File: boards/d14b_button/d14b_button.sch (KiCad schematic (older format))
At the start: 65 parts, among them CON1 USB-MICRO-B, P1 CONN_02X05, P2 CONN_01X03, P3 PIEZO_BUZZ, P4 EEPROM_SPI, Q1 MOSFET_N, Q2 IRLM6402, Q3 BSS138, SW1 SW_PUSH, SW2 SW_PUSH, SW3 SW_PUSH, SW4 SW_PUSH, U1 nRF24L01+-Module, U2 STM32F030C8T6, U3 TPS61221, X1 8M, X2 32.768k

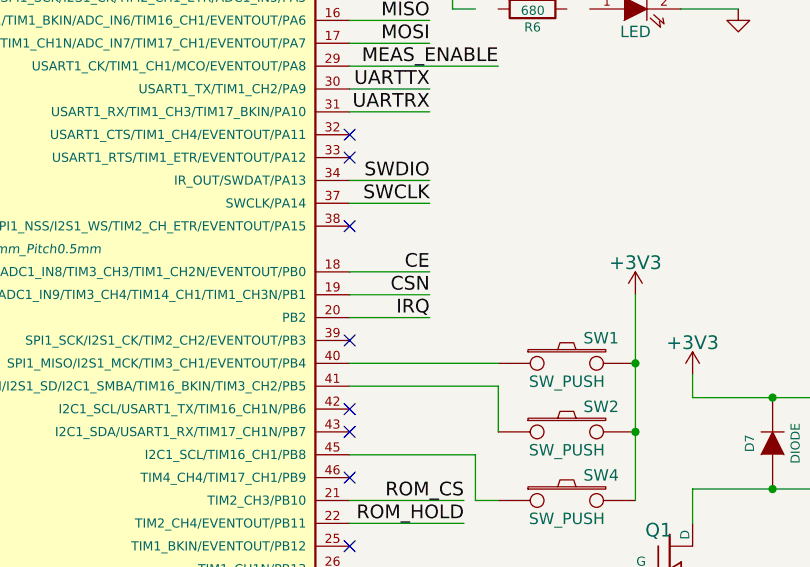
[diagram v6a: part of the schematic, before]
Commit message: Fiebermurks verworfen, Redesign der Platine angeworfen --> Revision 2, Interactive Routing ist geil :-)
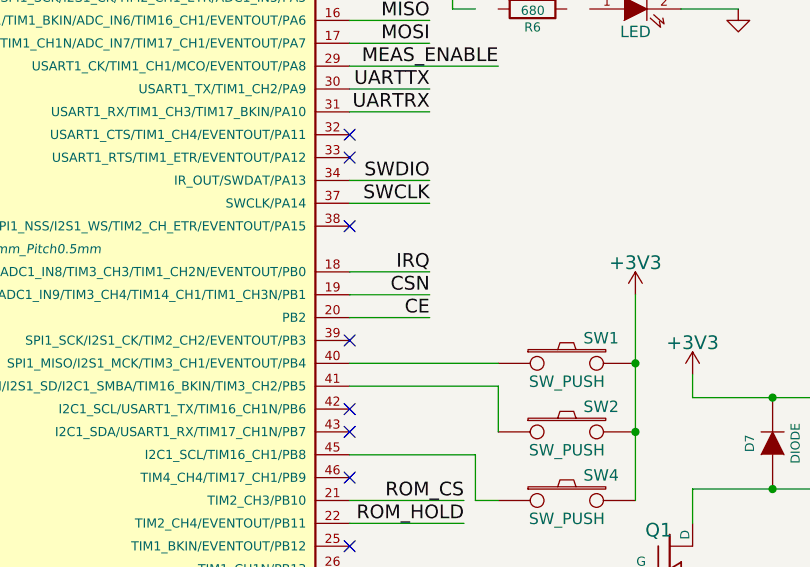
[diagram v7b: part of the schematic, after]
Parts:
- JP2: footprint Oddities:NetTie-II_SMD -> Connect:PINHEAD1-3
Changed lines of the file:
@@
 Text Label 5250 2750 2    60   ~ 0
 MOSI
-Text Label 5250 3750 2    60   ~ 0
+Text Label 5250 3950 2    60   ~ 0
 CE
 Text Label 5250 3850 2    60   ~ 0
 CSN
-Text Label 5250 3950 2    60   ~ 0
+Text Label 5250 3750 2    60   ~ 0
 IRQ
 Wire Wire Line
@@
 F 0 "JP2" H 7700 5950 40  0000 L CNN
 F 1 "JUMPER3" H 7650 6150 40  0000 C CNN
-F 2 "Oddities:NetTie-II_SMD" H 7650 6050 60  0001 C CNN
+F 2 "Connect:PINHEAD1-3" H 7650 6050 60  0001 C CNN
 F 3 "" H 7650 6050 60  0000 C CNN
 	1    7650 6050

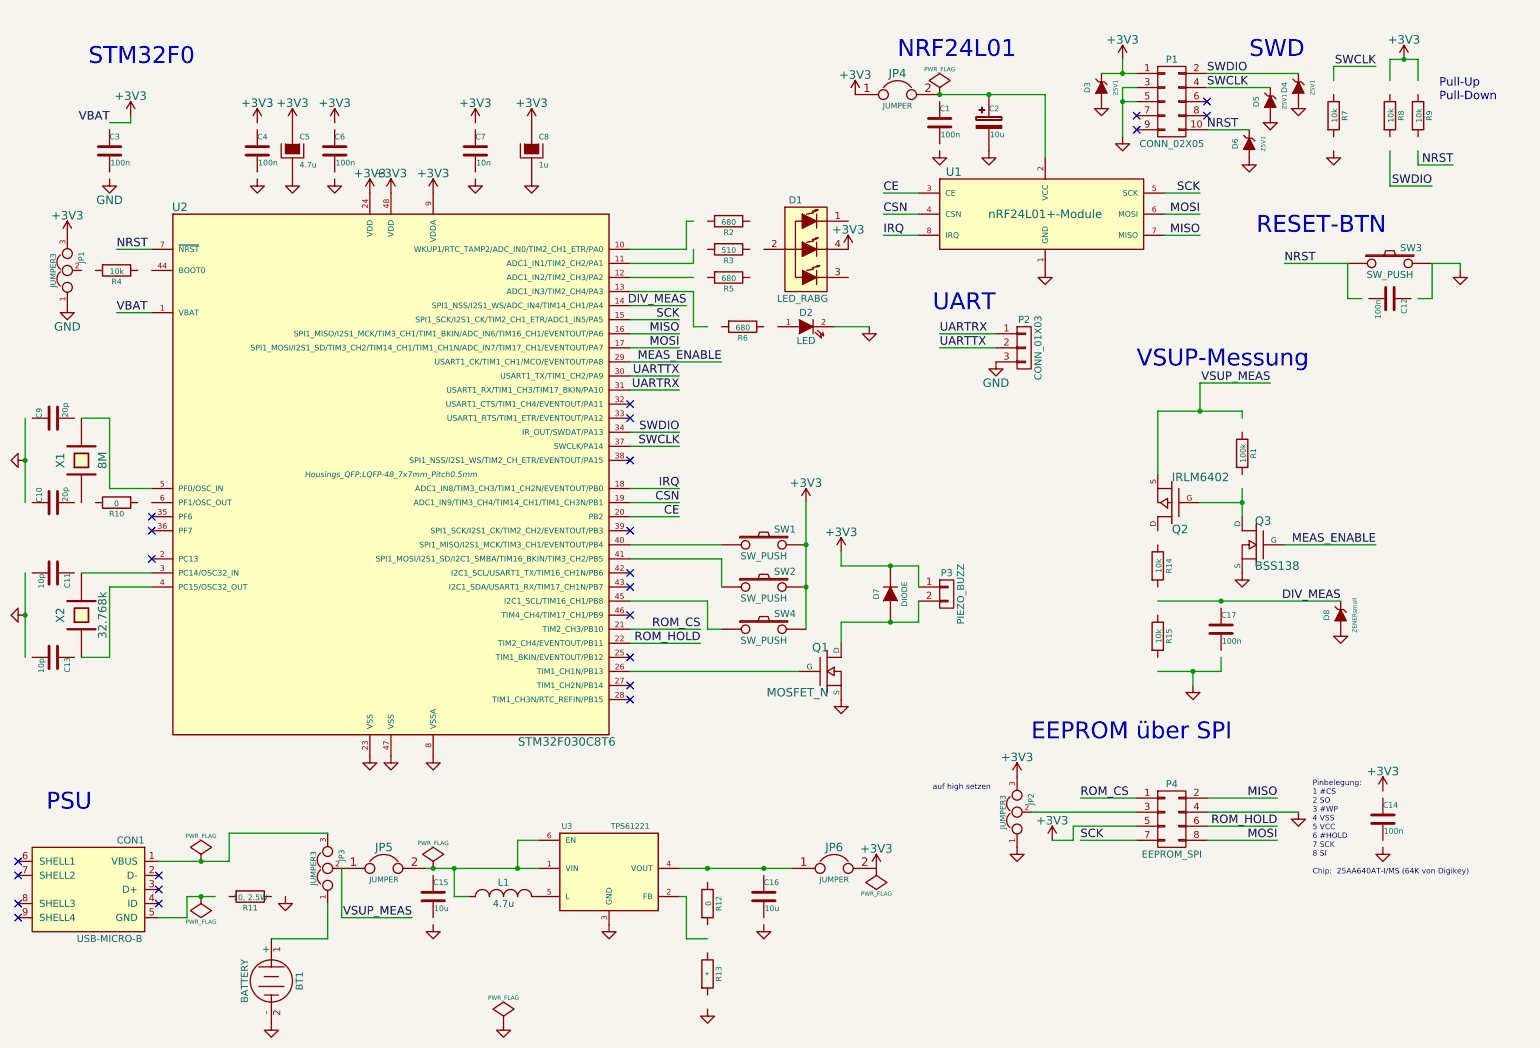
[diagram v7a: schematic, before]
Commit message: update schematic to new symbols and generate PDF
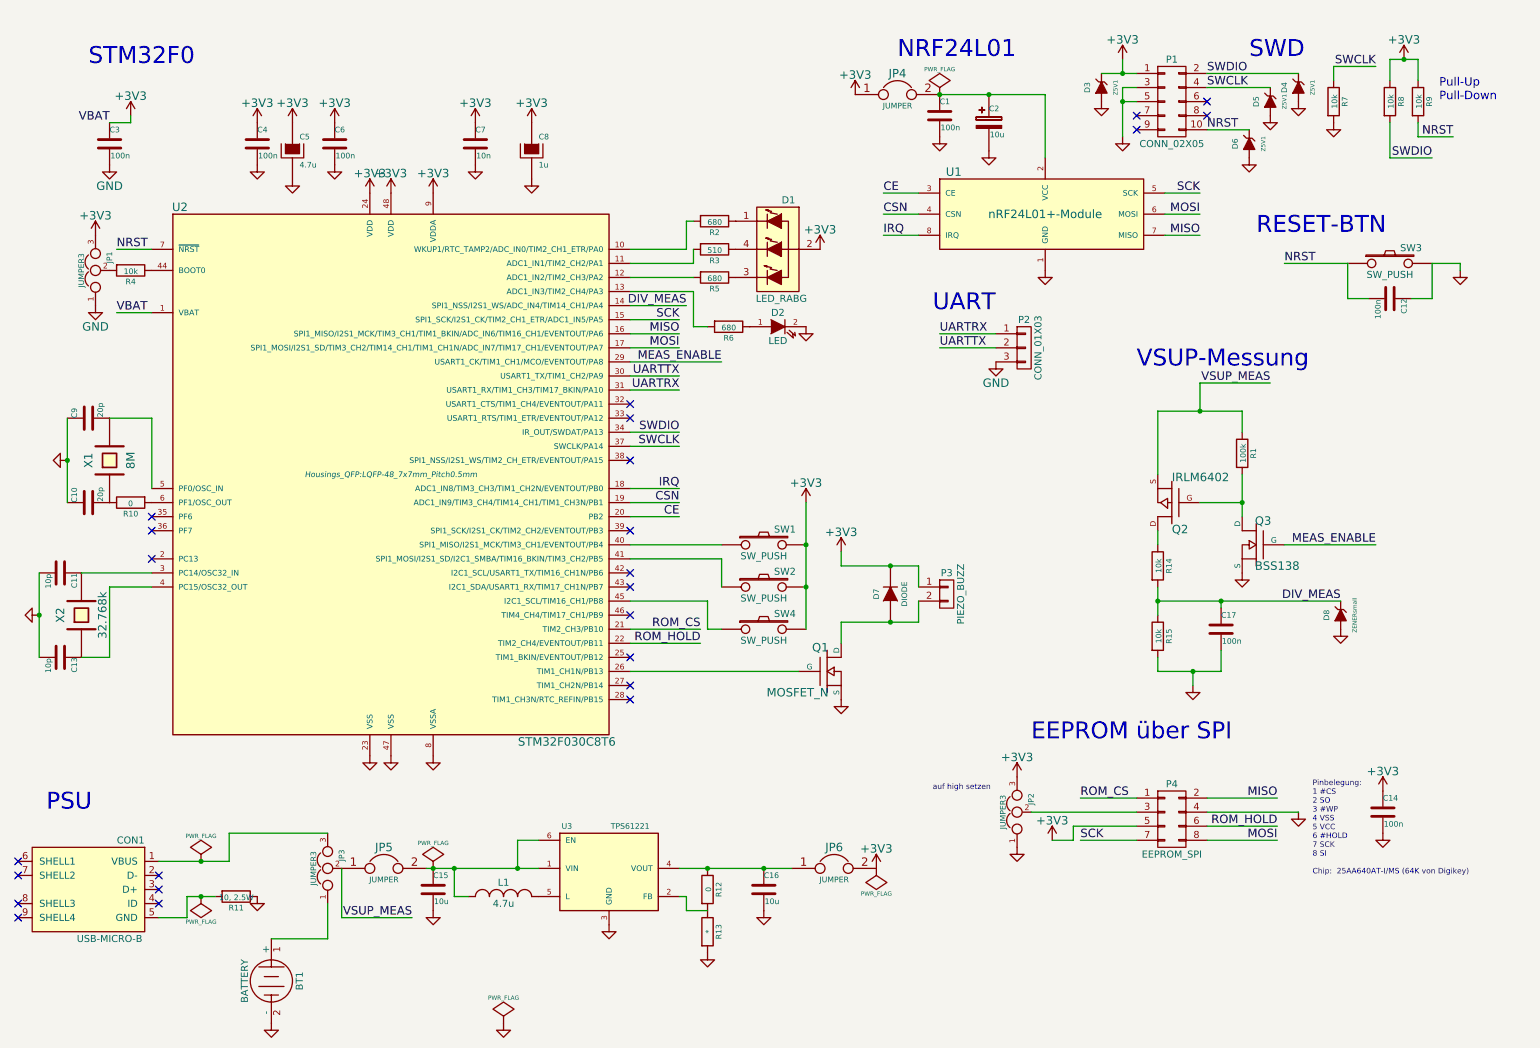
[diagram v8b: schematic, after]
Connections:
- wire segments 126 -> 128
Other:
- moved on the sheet: C1, C10, C11, C13, C14, C15, C16, C3, C4, C6, C7, C9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
